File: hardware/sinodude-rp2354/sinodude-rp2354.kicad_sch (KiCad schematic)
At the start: 93 parts, among them J1 USB-C, J2 SWD TC2030-IDC latching, J4 DUT, Q1 2N7002, SW1 BOOTSEL, SW2 RESET, U1 RP2354A, U2 AMS1117-3.3, U3 TPS2114APW, U4 SN74LVC8T245PW, U5 SN74LVC1T45DBV, U6 SN74LVC1T45DBV, Y1 12MHz/CL10pF/ESR50R/ABM8-272-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

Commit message: hardware: clear every DRC and ERC warning on the RP2354 board
The board reported 0 errors but 247 warnings and 12 "unconnected" items.
Both reports are now empty at every severity.

The unconnected items were not cosmetic. They were ratsnest lines between
ground pour regions, and ten GND pads sat in pockets of pour that reached
nothing else, so those pads were floating: U5 and U6's ground pins, the
crystal's, the ESD diode's, and six decoupling caps'. On two layers a dense
signal field cuts the pour into islands, and a pad stranded in one still reads
as routed unless you look at what the zone-to-zone line actually means.

Reconnecting them needed more than stitching vias:

- DATA_DIR is rerouted, which frees C32 and U5's ground pin.
- One 4.2 mm length of +3V3 east of U4 drops to 0.20 mm, opening the slot U5's
  ground escapes through. It carries the shifters' A-side supply, a few mA.
- The +3V3 climb between C6 and C12 moves, and the two caps' ground pads are
  tied directly, which is what finally reaches C12.

Also in the copper: dead track stubs and vias removed (a few were load-bearing
and were trimmed back to their junction instead), RUN's escape from its via
rebuilt as one 45 degree run, and seven segments snapped to exact 45 degrees.

The 89 library mismatches were real drift, not noise: the board's footprints
carried no `attr`, no 3D model, and float-rounded coordinates from an earlier
flip. All three are restored from the libraries, so the check is meaningful
again. Three footprints genuinely differ from stock and are now project copies
in footprints/sinodude.pretty: the USB-C receptacle (corner ground pads trimmed
to clear the shell holes), the DUT header (pin 1 arrow off R26's pad), and the
QFN (thermal vias at JLCPCB's minimum drill). J2 regains the stock keepout
zone, so "no via on a Tag-Connect pad" is enforced by the footprint.

The 53 silkscreen warnings are fixed by placing reference designators: they are
clear of pads and of each other, and all rea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
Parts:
- J1: footprint Connector_USB:USB_C_Receptacle_GCT_USB4105-xx-A_16P_TopMnt_Horizontal -> sinodude:USB_C_Receptacle_GCT_USB4105-xx-A_16P_TopMnt_Horizontal
- J4: footprint Connector_IDC:IDC-Header_2x05_P2.54mm_Horizontal -> sinodude:IDC-Header_2x05_P2.54mm_Horizontal
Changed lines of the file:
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@@
 			)
 		)
-		(property "Footprint" "Connector_USB:USB_C_Receptacle_GCT_USB4105-xx-A_16P_TopMnt_Horizontal"
+		(property "Footprint" "sinodude:USB_C_Receptacle_GCT_USB4105-xx-A_16P_TopMnt_Horizontal"
 			(at 34.29 76.2 0)
 			(hide yes)
@@
 			)
 		)
-		(property "Footprint" "Connector_IDC:IDC-Header_2x05_P2.54mm_Horizontal"
+		(property "Footprint" "sinodude:IDC-Header_2x05_P2.54mm_Horizontal"
 			(at 130.81 344.17 0)
 			(hide yes)

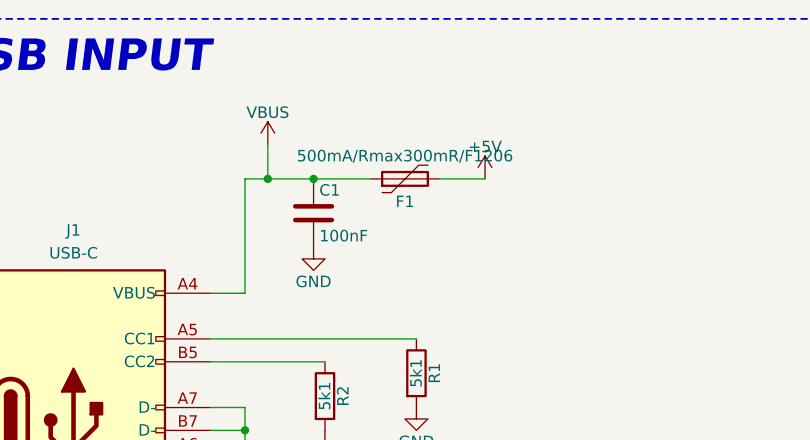
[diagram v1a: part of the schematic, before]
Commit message: hardware: cut both edges back so the connectors reach a case wall, 750 mA fuse
The board is 64 x 36 mm now, down from 68 x 36.

The west edge moves from x = 100 to 101.4, so J1's shell stands 1.4 mm proud
of the board instead of sitting flush with it. 1.4 mm is the geometric
maximum, not a choice: the receptacle's own shield tabs are plated slots
reaching x = 101.7 and the board has to hold them with 0.3 mm of copper
clearance. The east edge moves from 168 to 165.4, giving J4 2.1 mm of proud
shroud; that one could go further, since J4's pins stop at x = 157.6.

The four M3 holes now sit 3.2 mm in from both edges they meet, so each is on
its corner diagonal rather than 4.5 mm horizontally and 3.6 mm vertically.
3.2 mm is what U2's courtyard leaves for H3.

F1 becomes a Littelfuse 1206L075/16WR (C371166), 750 mA hold and 1.5 A trip,
in the same 1206 land. The 500 mA part it replaces held under 20% margin over
the 400 to 430 mA worst case before any ambient derating, sitting next to a
regulator burning 0.7 W. The new part is also lower resistance, 90 mohm
typical against 150. Its stock is thinner: about 6 k against 300 k.

Consequences absorbed: the outermost stitching via columns at x = 101.5 and
166.5 are gone with the copper they stood in, as is one via that the moved H2
crowded; J4's silk body outline is clipped at the edge it overhangs; J1's
reference designator moved back inside the board. Zone outlines follow the new
edges. DRC and ERC stay clean at every severity, GND is still one region, and
gerbers and drills still export.
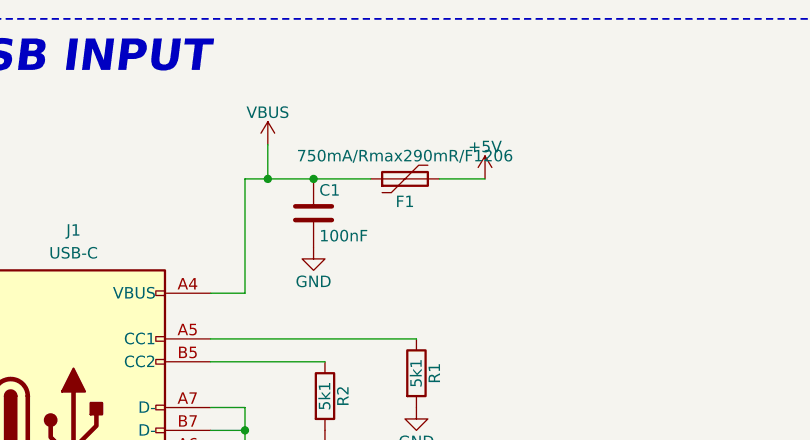
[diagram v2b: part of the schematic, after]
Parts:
- F1: value 500mA/Rmax300mR/F1206 -> 750mA/Rmax290mR/F1206; LCSC C720075 -> C371166
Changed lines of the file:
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@@
 			)
 		)
-		(property "Value" "500mA/Rmax300mR/F1206"
+		(property "Value" "750mA/Rmax290mR/F1206"
 			(at 71.12 45.72 90)
 			(show_name no)
@@
 			)
 		)
-		(property "LCSC" "C720075"
+		(property "LCSC" "C371166"
 			(at 71.12 48.26 90)
 			(hide yes)

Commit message: hardware: centre the board on the page and fill in both title blocks
The outline sat at x 101.4-165.4, y 102-138 on an A4 sheet, which put it up
and to the left of centre. Everything (93 footprints, 1182 track items, 8
drawings, both zones) moved by +15.1, -15.0 mm, so the outline is now
116.5-180.5 by 87-123 and its centre lands on the A4 centre exactly.

The PCB had no title block at all. Both documents now carry the same one:
title, date, rev A, company, and the four comment lines the schematic already
had. The README's edge description loses its absolute coordinates, which this
move has just shown to be the wrong thing to write down; the distances that
actually matter stay.

DRC and ERC clean at every severity, GND still one region, tracks still on
0/45/90.
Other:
- company: (none) -> carlossless
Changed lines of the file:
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@@
 	(title_block
 		(title "sinodude-rp2354")
+		(date "2026-09-16")
 		(rev "A")
+		(company "carlossless")
 		(comment 1 "USB ICP programmer for SinoWealth 8051 microcontrollers")
 		(comment 2 "DUT header pin-compatible with SinoLink V2.2")

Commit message: hardware: name header pin 7 TDA, not KEY
SinoWealth's tool-selection note tabulates adapter signals per target
core: ARM gets SWD (VDD SWCLK SWDIO GND), Andes gets AICE
(VDD TCK TDA GND), and the 8051 parts get VDD TCK TDI TDO GND. The 2x5
header carries both styles at once, so pin 7 is the Andes AICE data
wire sharing TCK with the 8051 path. It was carried over from SinoLink
as an unexplained "KEY" line.

Renames KEY_3V3, KEY_B and KEY_DIR to TDA_3V3, TDA_B and TDA_DIR.

Also corrects the GPIO map, which had DATA and KEY on each other's
translators and implied GPIO2 was TCK. The schematic wires GPIO2-5 to
nRST, TMS, TDI, TCK in that order, GPIO6/7 to U6 and GPIO8/9 to U5.
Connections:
- net KEY_3V3 renamed TDA_3V3
- net KEY_B renamed TDA_B
- net KEY_DIR renamed TDA_DIR
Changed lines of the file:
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@@
 		)
 	)
-	(global_label "KEY_3V3"
+	(global_label "TDA_3V3"
 		(shape input)
 		(at 513.08 269.24 180)
@@
 		)
 	)
-	(global_label "KEY_B"
+	(global_label "TDA_B"
 		(shape input)
 		(at 533.4 269.24 0)
@@
 		)
 	)
-	(global_label "KEY_B"
+	(global_label "TDA_B"
 		(shape input)
 		(at 85.09 368.3 180)
@@
 		)
 	)
-	(global_label "KEY_DIR"
+	(global_label "TDA_DIR"
 		(shape input)
 		(at 502.92 274.32 180)
@@
 		)
 	)
-	(global_label "KEY_3V3"
+	(global_label "TDA_3V3"
 		(shape input)
 		(at 105.41 217.17 0)
@@
 		)
 	)
-	(global_label "KEY_DIR"
+	(global_label "TDA_DIR"
 		(shape input)
 		(at 105.41 219.71 0)

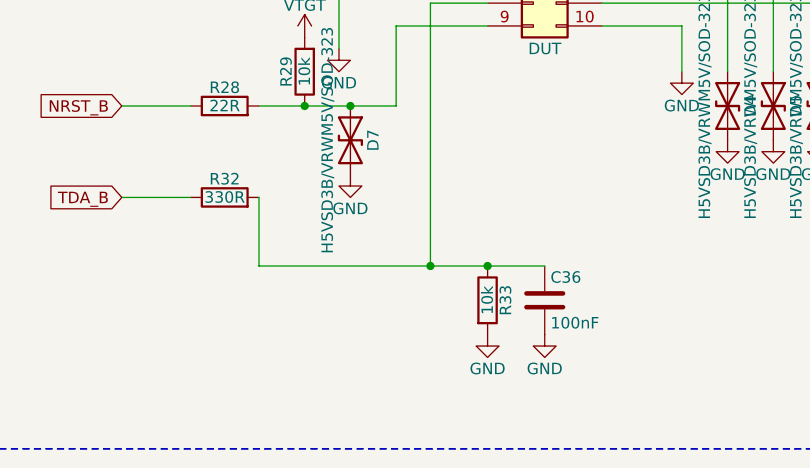
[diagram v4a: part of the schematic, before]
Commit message: hardware: make TDA a working data line
Header pin 7 carried a 330 R series resistor and a fitted 100 nF to
ground, a 33 us low-pass on a wire whose whole protocol is edge timing,
plus a 10 k pull-down where the other two bidirectional lines pull up,
and it was the only target signal with no ESD clamp.

Those passives came from reading SinoLink's DUT sheet wrong. Neither is
on SinoLink's TDA: its cap position C28 carries the value DNI and is not
fitted, and the only 330 R on that sheet is a transistor-switched
pull-up on TDO, a different pin. SinoLink does clamp TDA, with D9.

So pin 7 now matches nRST and DATA exactly:

- C36 deleted; D9 (H5VSD3B) takes its footprint, keeping the D7/D8/D9
  clamp row aligned
- R32 330 R to 22 R, the value every other target line uses
- R33 repointed from GND to VTGT, matching R29 and R31
- the GND stitching via that touched R33's far pad moved 1 mm clear,
  now that the pad is no longer ground

DRC and ERC clean at every severity, no unconnected items, no schematic
parity errors, 88 placed parts unchanged, every track still on 0/45/90
with every pad entered at its centre.
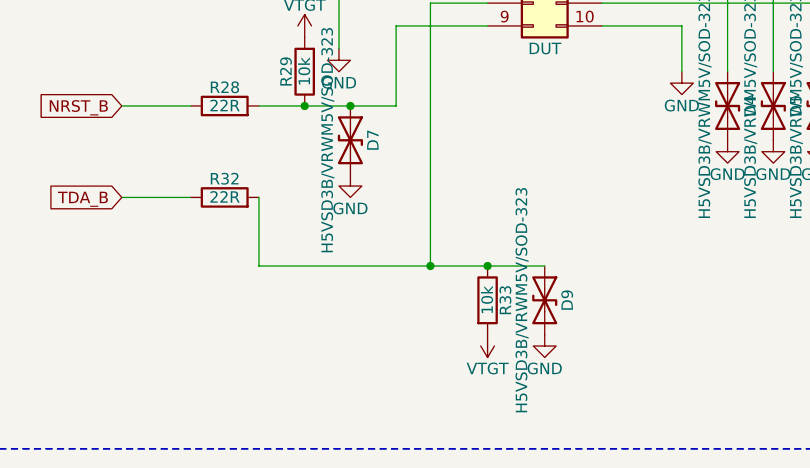
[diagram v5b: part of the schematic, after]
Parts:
- removed C36: 100nF, Capacitor_SMD:C_0603_1608Metric, symbol Device:C
- added D9: H5VSD3B/VRWM5V/SOD-323, Diode_SMD:D_SOD-323, symbol Device:D_TVS
- R32: value 330R -> 22R; LCSC C23138 -> C23345
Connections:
- net GND: now also D9.2 (A2); no longer R33.2
- net VTGT: now also R33.2
- net at J4.7 (Pin_7), R32.2, R33.1: now also D9.1 (A1)
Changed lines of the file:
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@@
 	)
 	(symbol
-		(lib_id "Device:C")
-		(at 132.08 379.73 0)
-		(unit 1)
-		(exclude_from_sim no)
-		(in_bom yes)
-		(on_board yes)
-		(dnp no)
-		(property "Reference" "C36"
-			(at 132.715 377.19 0)
-			(show_name no)
-			(do_not_autoplace no)
-			(effects
-				(font
-					(size 1.27 1.27)
-				)
-				(justify left)
-			)
-		)
-		(property "Value" "100nF"
-			(at 132.715 382.27 0)
-			(show_name no)
-			(do_not_autoplace no)
-			(effects
-				(font
-					(size 1.27 1.27)
-				)
-				(justify left)
-			)
-		)
-		(property "Footprint" "Capacitor_SMD:C_0603_1608Metric"
-			(at 132.08 379.73 0)
-			(hide yes)
-			(show_name no)
-			(do_not_autoplace no)
-			(effects
-				(font
-					(size 1.27 1.27)
-				)
-			)
-		)
-		(property "Datasheet" ""
-			(at 132.08 379.73 0)
-			(hide yes)
-			(show_name no)
-			(do_not_autoplace no)
-			(effects
-				(font
-					(size 1.27 1.27)
-				)
-			)
-		)
-		(property "Description" "Unpolarized capacitor"
-			(at 132.08 379.73 0)
-			(hide yes)
-			(show_name no)
-			(do_not_autoplace no)
-			(effects
-				(font
-					(size 1.27 1.27)
-				)
-			)
-		)
-		(property "LCSC" "C14663"
-			(at 132.08 379.73 0)
-			(hide yes)
-			(show_name no)
-			(do_not_autoplace no)
-			(effects
-				(font
-					(size 1.27 1.27)
-				)
-			)
-		)
-		(body_style 1)
-		(in_pos_files yes)
-		(pin "1"
-		)
-		(pin "2"
-		)
-		(instances
-			(project "sinodude-rp2354"
-				(path "/a3e36d10-b615-4e51-a27d-75418708c944"
-					(reference "C36")
-					(unit 1)
-				)
-			)
-		)
-	)
-	(symbol
 		(lib_id "power:VCC")
 		(at 171.45 379.73 180)
@@
 	)
 	(symbol
-		(lib_id "power:GND")
-		(at 125.73 383.54 0)
+		(lib_id "power:VCC")
+		(at 125.73 383.54 180)
 		(unit 1)
 		(exclude_from_sim no)
@@
 			)
 		)
-		(property "Value" "GND"
+		(property "Value" "VTGT"
 			(at 125.73 387.35 0)
 			(show_name no)
@@
 			)
 		)
-		(property "Description" "Power symbol creates a global label with name \"GND\" , ground"
+		(property "Description" "Power symbol creates a global label with name \"VCC\""
 			(at 125.73 383.54 0)
 			(hide yes)
@@
 			)
 		)
-		(property "Value" "330R"
+		(property "Value" "22R"
 			(at 96.52 368.3 90)
 			(show_name no)
@@
 			)
 		)
-		(property "LCSC" "C23138"
+		(property "LCSC" "C23345"
 			(at 96.52 368.3 90)
 			(hide yes)
@@
 		)
 	)
+	(symbol
+		(lib_id "Device:D_TVS")
+		(at 132.08 379.73 270)
+		(unit 1)
+		(in_bom yes)
+		(on_board yes)
+		(dnp no)
+		(property "Reference" "D9"
+			(at 134.62 379.73 0)
+			(effects
+				(font
+					(size 1.27 1.27)
+				)
+			)
+		)
+		(property "Value" "H5VSD3B/VRWM5V/SOD-323"
+			(at 129.54 379.73 0)
+			(effects
+				(font
+					(size 1.27 1.27)
+				)
+			)
+		)
+		(property "Footprint" "Diode_SMD:D_SOD-323"
+			(at 132.08 379.73 0)
+			(hide yes)
+			(effects
+				(font
+					(size 1.27 1.27)
+				)
+			)
+		)
+		(property "Datasheet" ""
+			(at 132.08 379.73 0)
+			(hide yes)
+			(effects
+				(font
+					(size 1.27 1.27)
+				)
+			)
+		)
+		(property "Description" "Bidirectional transient-voltage-suppression diode"
+			(at 132.08 379.73 0)
+			(hide yes)
+			(effects
+				(font
+					(size 1.27 1.27)
+				)
+			)
+		)
+		(instances
+			(project "sinodude-rp2354"
+				(path "/a3e36d10-b615-4e51-a27d-75418708c944"
+					(reference "D9")
+					(unit 1)
+				)
+			)
+		)
+		(property "LCSC" "C20615806"
+			(at 132.08 379.73 0)
+			(hide yes)
+			(effects
+				(font
+					(size 1.27 1.27)
+				)
+			)
+		))
 	(polyline
 		(pts

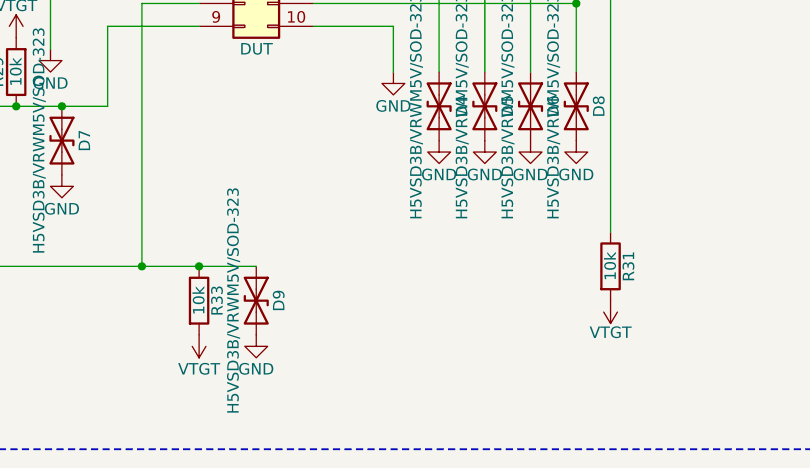
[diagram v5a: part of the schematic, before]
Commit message: hardware: strengthen the data-line pull-ups for protoB and SWD
SinoLink runs four wire protocols over this header: protoA JTAG
bit-bang, protoB single-wire pulse-width, CMSIS-DAP SWD, and Andes
AICE. All four are carried here already, now that TDA works: the three
lines that reverse sit on their own translator with a GPIO DIR, and the
four that never reverse share U4.

The one thing that did not carry over was pull-up strength. SinoLink
translates its data wire with a PCA9306, a passive pass-FET that cannot
drive high, so its 1k on the MCU side and switched 330R on the target
side are its high-side driver rather than a bus bias. The SN74LVC1T45
here is push-pull and drives high on its own, so no switched pull-up is
wanted; what is left is the released line, where the target drives
open-drain and the resistor alone sets the rising edge.

R31 and R33 go 10k to 1k, matching SinoLink's static value: about 30 ns
into the ~30 pF a short ribbon presents, against ~300 ns at 10k, which
matters where the protocol is decoded by measuring pulse widths. R29 on
nRST stays 10k, since a reset line is not clocked.

Also corrects F1's stated margin. U3's limit is not a flat 333 mA:
scaling the datasheet's 700 ohm row to R15 = 750 ohm gives
280 / 336 / 467 mA, so the worst case through F1 is ~540 mA, not the
400-430 mA claimed. Still inside the 750 mA hold.
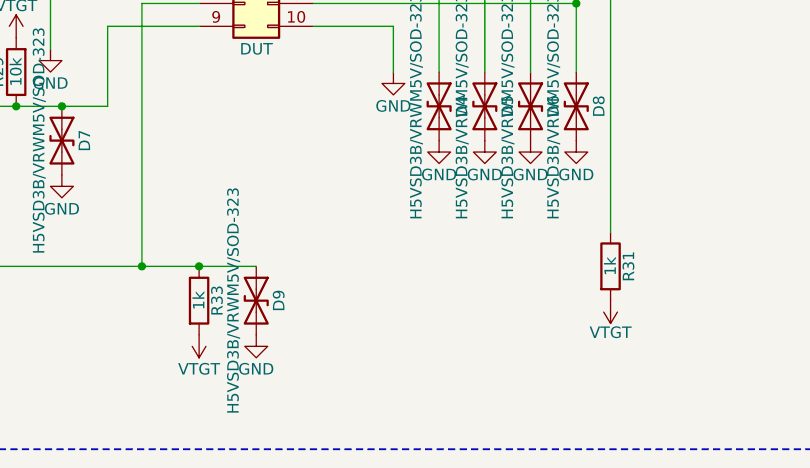
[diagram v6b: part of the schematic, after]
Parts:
- R31, R33: value 10k -> 1k; LCSC C25804 -> C21190
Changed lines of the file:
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@@
 			)
 		)
-		(property "Value" "10k"
+		(property "Value" "1k"
 			(at 125.73 379.73 90)
 			(show_name no)
@@
 			)
 		)
-		(property "LCSC" "C25804"
+		(property "LCSC" "C21190"
 			(at 125.73 379.73 0)
 			(hide yes)
@@
 			)
 		)
-		(property "Value" "10k"
+		(property "Value" "1k"
 			(at 171.45 375.92 90)
 			(show_name no)
@@
 			)
 		)
-		(property "LCSC" "C25804"
+		(property "LCSC" "C21190"
 			(at 171.45 375.92 0)
 			(hide yes)
